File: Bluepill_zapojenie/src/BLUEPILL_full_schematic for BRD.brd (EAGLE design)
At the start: 40.6 x 67 mm, 8 parts

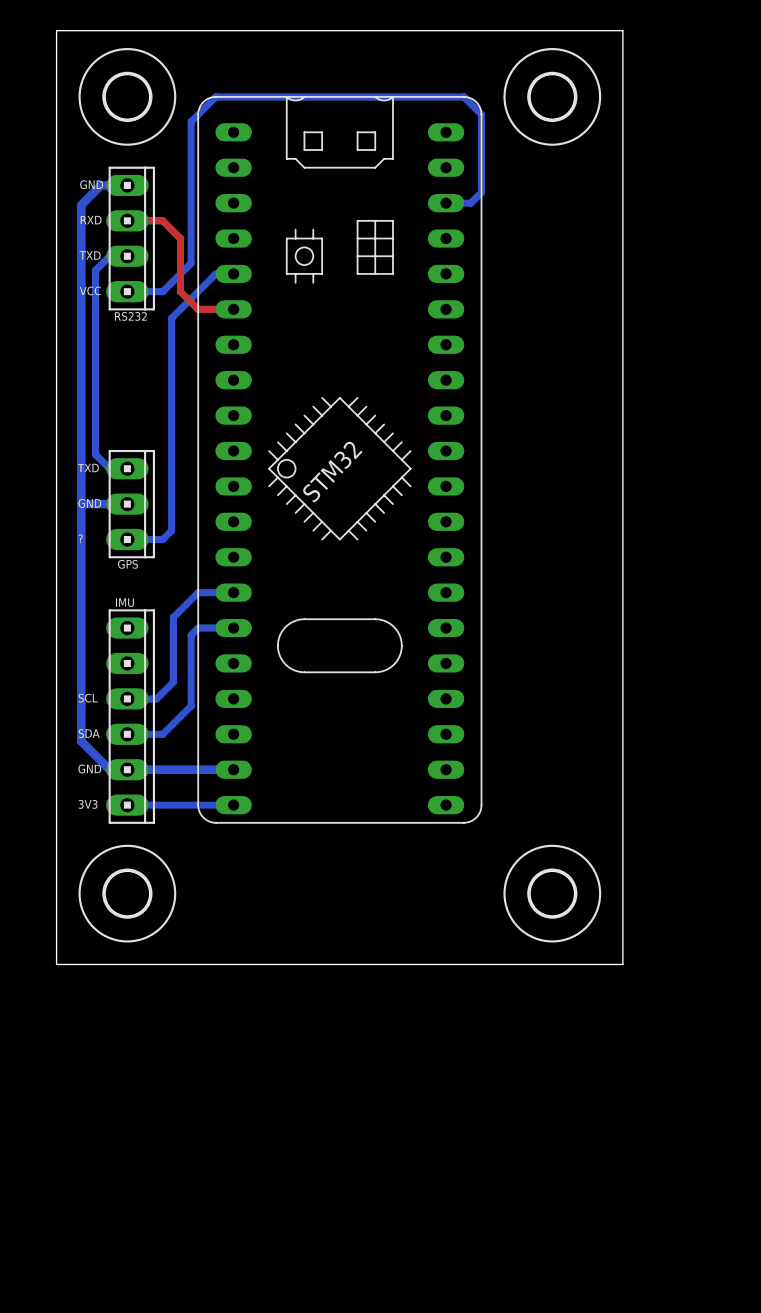
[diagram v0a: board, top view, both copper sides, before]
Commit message: BRD schema final version
added IMU to PCB + CAM and UART connectors. 5V VCC from USB to Bluepill
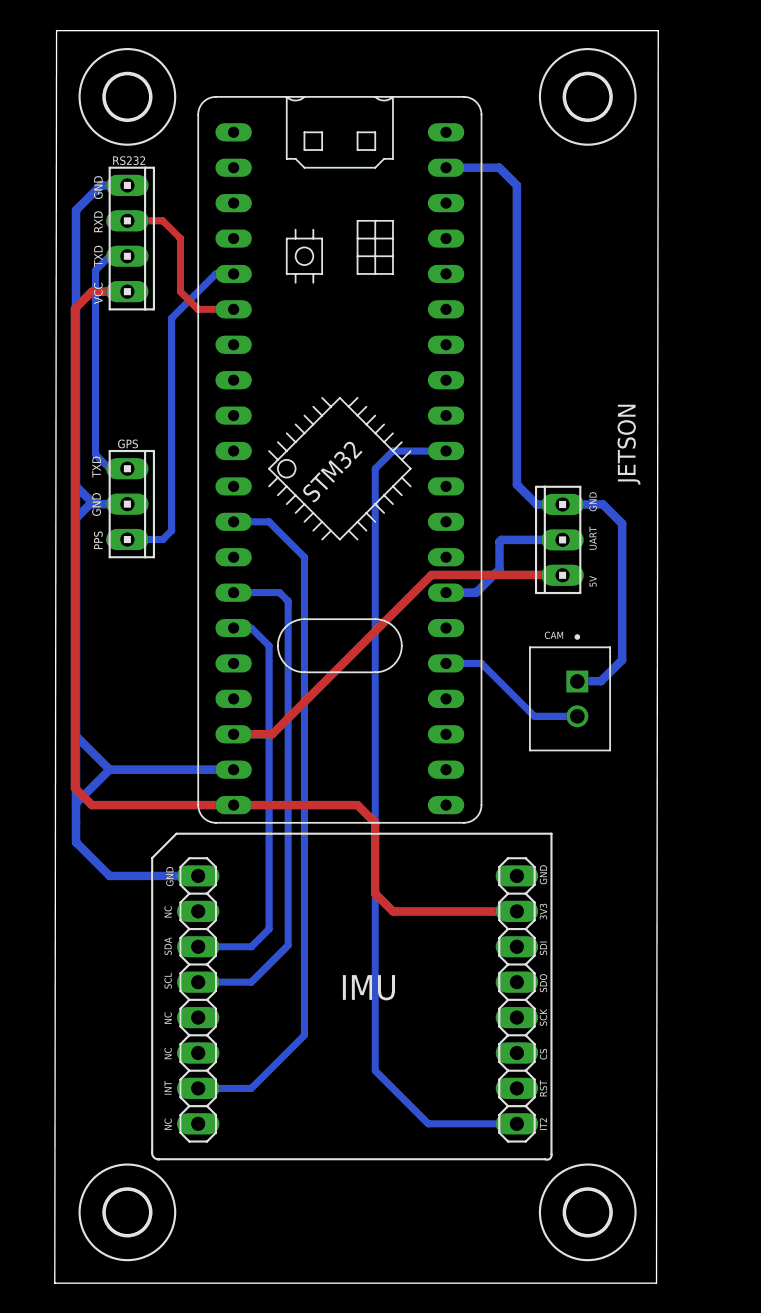
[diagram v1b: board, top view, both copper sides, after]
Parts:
- removed IMU: (no value), con-amp:10X06MTA
- added CAM: B2B-XH-A, B2B-XH-A Model:JST_B2B-XH-A
- added JETSON: (no value), con-amp:10X03MTA
- added JP1, JP2: (no value), pinhead:1X08
- moved U$4 23.0 mm to (38.1, 15.2)
- moved U$3 22.9 mm to (5.08, 15.2)
- moved U$2 2.54 mm to (38.1, 95.2)
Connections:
- net N$2 renamed PPS
- removed net VCC: MOD1.P$23, RS232.1
- new net 5V: JETSON.3, MOD1.P$18
- new net DRDY: JP2.2, MOD1.P$12
- new net FSYNC: JP1.1, MOD1.P$30
- new net GND2: CAM.1, JETSON.1, MOD1.P$22
- new net N$6: CAM.2, MOD1.P$36
- new net UART: JETSON.2, MOD1.P$34
- net 3V3: now also JP1.7, RS232.1; no longer IMU.1
- net GND: now also JP2.8; no longer IMU.2
- net SCL: now also JP2.5; no longer IMU.4
- net SDA: now also JP2.6; no longer IMU.3
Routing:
- net 3V3: track 7.62 -> 77.0 mm
- net FSYNC: track 0.00 -> 60.5 mm
- net DRDY: track 0.00 -> 49.6 mm
- net GND2: track 0.00 -> 49.4 mm
- net VCC: track 46.1 -> 0.00 mm
- net 5V: track 0.00 -> 28.3 mm
- net GND: track 57.4 -> 81.1 mm
- net SCL: track 13.5 -> 36.4 mm
- net SDA: track 13.8 -> 29.0 mm
- net UART: track 0.00 -> 11.1 mm
- net N$6: track 0.00 -> 11.0 mm
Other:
- board size 40.6 x 67 mm -> 43.3 x 89.8 mm
- board text added: "5V"
- board text added: "CS"
- board text added: "IMU"
- board text added: "INT"
- board text added: "IT2"
- board text added: "NC"
- board text added: "PPS"
- board text added: "RST"
- board text added: "SCK"
- board text added: "SDI"
- board text added: "SDO"
- board text added: "UART"
- board text removed: "?"

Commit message: Final push
schemy, exporty final verzie
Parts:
- added 5V, 5V_STM: (no value), pinhead:1X01
- moved GPS 6.70 mm to (4.88, 72.7)
- moved U$4 5.87 mm to (43.9, 14.3)
- moved U$2 5.84 mm to (43.9, 96.0)
- moved JP1 4.12 mm to (34.0, 26.5)
- moved JP2 4.12 mm to (11.2, 26.5)
- moved U$1 2.79 mm to (2.38, 96.0)
- moved U$3 2.38 mm to (2.78, 14.6)
- moved CAM 2.00 mm to (36.8, 50.1)
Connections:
- removed net 5V: JETSON.3, MOD1.P$18
- removed net GND2: CAM.1, JETSON.1, MOD1.P$22
- new net N$2: 5V_STM.1, MOD1.P$18
- new net N$3: 5V.1, JETSON.3
- net 3V3: now also MOD1.P$23, RS232.4; no longer MOD1.P$20, RS232.1
- net GND: now also CAM.2, GPS.3, JETSON.1, RS232.1; no longer GPS.2, RS232.4
- net N$6: now also CAM.1; no longer CAM.2
- net TXD: now also GPS.2; no longer GPS.3
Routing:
- net GND: track 81.1 -> 0.00 mm
- net GND2: track 49.4 -> 0.00 mm
- net 3V3: track 77.0 -> 116.0 mm
- net RXD: track 12.5 -> 44.6 mm
- net 5V: track 28.3 -> 0.00 mm
- net FSYNC: track 60.5 -> 78.1 mm
- net DRDY: track 49.6 -> 58.9 mm
- net SCL: track 36.4 -> 44.2 mm
- net SDA: track 29.0 -> 36.1 mm
- net PPS: track 24.4 -> 18.3 mm
- net N$2: track 0.00 -> 4.99 mm
- net N$3: track 0.00 -> 3.61 mm
- net TXD: track 18.6 -> 16.2 mm
- added copper zone on layer 16, net GND
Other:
- board size 43.3 x 89.8 mm -> 50.6 x 90 mm
